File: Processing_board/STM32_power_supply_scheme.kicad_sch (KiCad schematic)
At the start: 16 parts

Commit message: added reset button
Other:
- company: (none) -> N-Pulse
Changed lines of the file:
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@@
 	(generator_version "9.0")
 	(paper "A4")
+	(title_block
+		(company "N-Pulse")
+	)
 	(text "Correct to connect VDDA to VDD ?\n\"The VDDA voltage level is independent from the VDD voltage\n and must be connected to VDD (preferably) or to VSS pin when\n these peripherals are not used.\" datasheet p29\n"
 		(exclude_from_sim no)

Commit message: 3 RF antennas
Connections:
- net 3.3V renamed +3.3V
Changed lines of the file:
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@@
-		)
-	)
-	(global_label "3.3V"
-		(shape input)
-		(at 83.82 24.13 90)
-		(fields_autoplaced yes)
-		(effects
-			(font
-				(size 1.27 1.27)
-			)
-			(justify left)
-		)
-		(property "Intersheetrefs" "${INTERSHEET_REFS}"
-			(at 83.82 17.0324 90)
-			(effects
-				(font
-					(size 1.27 1.27)
-				)
-				(justify left)
-				(hide yes)
-			)
 		)
 	)
@@
 					(unit 1)
 				)
+			)
+		)
+	)
+	(symbol
+		(lib_id "power:+3.3V")
+		(at 83.82 24.13 0)
+		(unit 1)
+		(exclude_from_sim no)
+		(in_bom yes)
+		(on_board yes)
+		(dnp no)
+		(fields_autoplaced yes)
+		(property "Reference" "#PWR046"
+			(at 83.82 27.94 0)
+			(effects
+				(font
+					(size 1.27 1.27)
+				)
+				(hide yes)
+			)
+		)
+		(property "Value" "+3.3V"
+			(at 83.82 19.05 0)
+			(effects
+				(font
+					(size 1.27 1.27)
+				)
+			)
+		)
+		(property "Footprint" ""
+			(at 83.82 24.13 0)
+			(effects
+				(font
+					(size 1.27 1.27)
+				)
+				(hide yes)
+			)
+		)
+		(property "Datasheet" ""
+			(at 83.82 24.13 0)
+			(effects
+				(font
+					(size 1.27 1.27)
+				)
+				(hide yes)
+			)
+		)
+		(property "Description" "Power symbol creates a global label with name \"+3.3V\""
+			(at 83.82 24.13 0)
+			(effects
+				(font
+					(size 1.27 1.27)
+				)
+				(hide yes)
+			)
+		)
+		(pin "1"
+		)
+		(instances
+			(project "Processing_board"
+				(path "/b48cfd4a-6c36-4270-b2b4-45cb26e35477/dd373a49-14d9-4e57-878b-300a3ee89b4f"
+					(reference "#PWR046")
+					(unit 1)
+				)

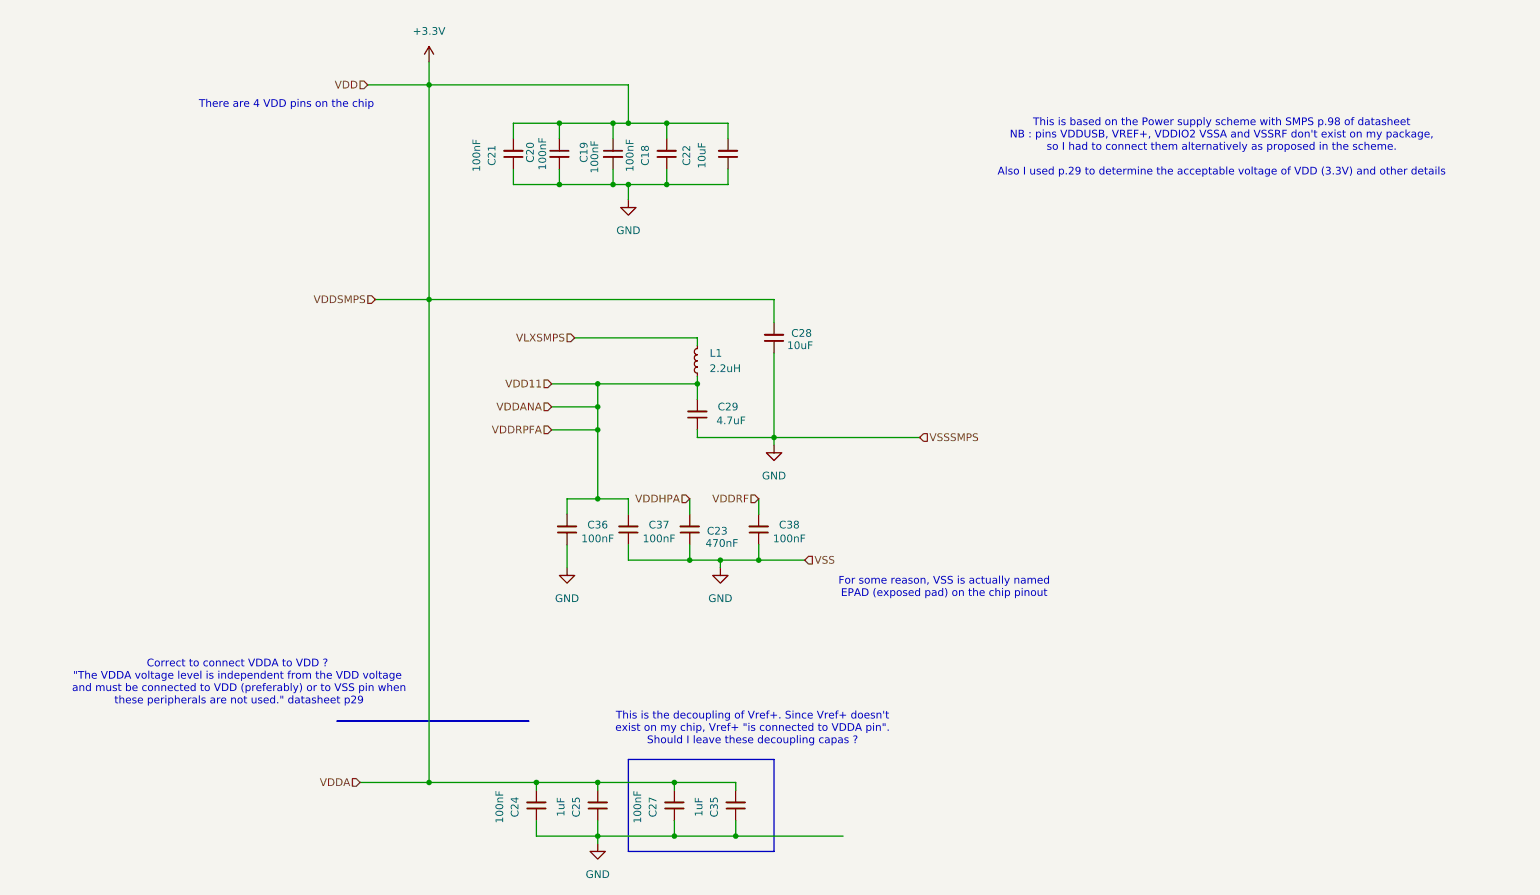
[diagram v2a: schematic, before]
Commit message: added all footprints, ready (?) to design PCB
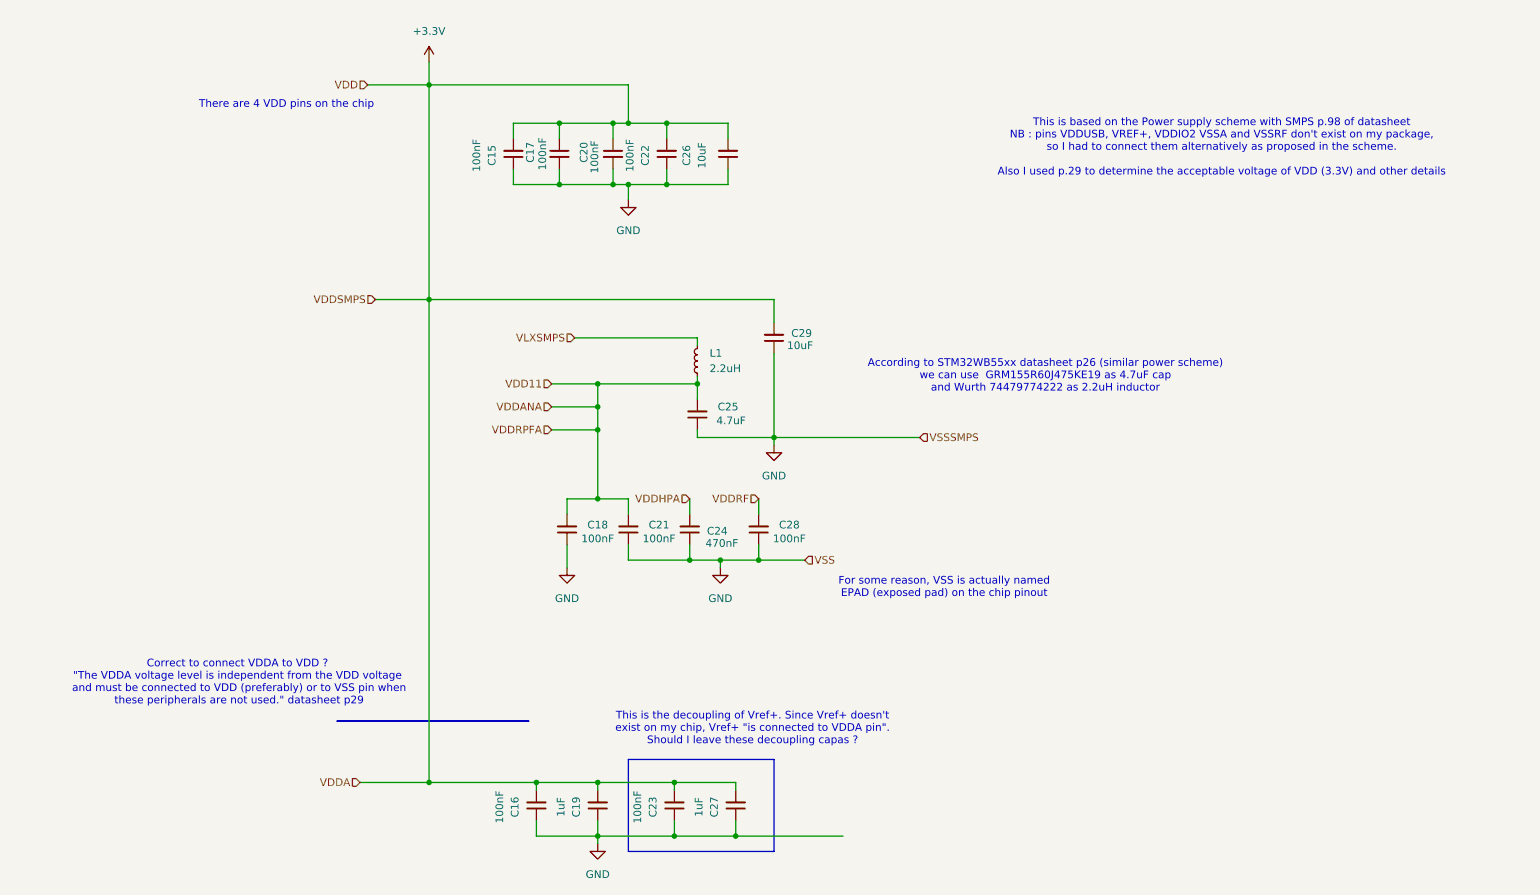
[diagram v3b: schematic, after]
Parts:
- C15: renamed from C21; footprint (none) -> Capacitor_SMD:C_0402_1005Metric
- C16: renamed from C24; footprint (none) -> Capacitor_SMD:C_0402_1005Metric
- C17: renamed from C20; footprint (none) -> Capacitor_SMD:C_0402_1005Metric
- C18: renamed from C36; footprint (none) -> Capacitor_SMD:C_0402_1005Metric
- C19: renamed from C25; footprint (none) -> Capacitor_SMD:C_0402_1005Metric
- C20: renamed from C19; footprint (none) -> Capacitor_SMD:C_0402_1005Metric
- C21: renamed from C37; footprint (none) -> Capacitor_SMD:C_0402_1005Metric
- C22: renamed from C18; footprint (none) -> Capacitor_SMD:C_0402_1005Metric
- C23: renamed from C27; footprint (none) -> Capacitor_SMD:C_0402_1005Metric
- C24: renamed from C23; footprint (none) -> Capacitor_SMD:C_0402_1005Metric
- C25: renamed from C29; footprint (none) -> Capacitor_SMD:C_0402_1005Metric
- C26: renamed from C22; footprint (none) -> Capacitor_SMD:C_0402_1005Metric
- C27: renamed from C35; footprint (none) -> Capacitor_SMD:C_0402_1005Metric
- C28: renamed from C38; footprint (none) -> Capacitor_SMD:C_0402_1005Metric
- C29: renamed from C28; footprint (none) -> Capacitor_SMD:C_0402_1005Metric
- L1: footprint (none) -> Inductor_SMD:L_0805_2012Metric
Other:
- note added: "According to STM32WB55xx datasheet p26 (similar power scheme) we can use GRM155R60J475KE19 as 4.7uF cap and Wurth 74479774222 as 2.2uH inductor"

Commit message: first draft of PCB almost done
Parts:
- removed C23: 100nF, Capacitor_SMD:C_0402_1005Metric, symbol Device:C_Small
- removed C27: 1uF, Capacitor_SMD:C_0402_1005Metric, symbol Device:C_Small
- renumbered C24 to C23, C25 to C24, C26 to C25, C28 to C26, C29 to C27
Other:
- note removed: "This is the decoupling of Vref+. Since Vref+ doesn't exist on my chip, Vref+ "is connected to VDDA pin". Should I leave these decoupling capas ?"
- moved on the sheet: C18

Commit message: more minor cleanup
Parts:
- renumbered C18 to C17, C17 to C18
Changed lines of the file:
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@@
 		(dnp no)
 		(fields_autoplaced yes)
-		(property "Reference" "#PWR066"
+		(property "Reference" "#PWR032"
 			(at 83.82 63.5 0)
 			(effects
@@
 			(project "Processing_board"
 				(path "/b48cfd4a-6c36-4270-b2b4-45cb26e35477/dd373a49-14d9-4e57-878b-300a3ee89b4f"
-					(reference "#PWR066")
+					(reference "#PWR032")
 					(unit 1)
 				)
@@
 		(dnp no)
 		(fields_autoplaced yes)
-		(property "Reference" "#PWR031"
+		(property "Reference" "#PWR034"
 			(at 104.14 114.3 0)
 			(effects
@@
 			(project "Processing_board"
 				(path "/b48cfd4a-6c36-4270-b2b4-45cb26e35477/dd373a49-14d9-4e57-878b-300a3ee89b4f"
-					(reference "#PWR031")
+					(reference "#PWR034")
 					(unit 1)
 				)
@@
 		(on_board yes)
 		(dnp no)
-		(property "Reference" "C18"
+		(property "Reference" "C17"
 			(at 109.22 100.838 0)
 			(effects
@@
 			(project "Processing_board"
 				(path "/b48cfd4a-6c36-4270-b2b4-45cb26e35477/dd373a49-14d9-4e57-878b-300a3ee89b4f"
-					(reference "C18")
+					(reference "C17")
 					(unit 1)
 				)
@@
 		(dnp no)
 		(fields_autoplaced yes)
-		(property "Reference" "#PWR035"
+		(property "Reference" "#PWR038"
 			(at 140.97 93.98 0)
 			(effects
@@
 			(project "Processing_board"
 				(path "/b48cfd4a-6c36-4270-b2b4-45cb26e35477/dd373a49-14d9-4e57-878b-300a3ee89b4f"
-					(reference "#PWR035")
+					(reference "#PWR038")
 					(unit 1)
 				)
@@
 		(dnp no)
 		(fields_autoplaced yes)
-		(property "Reference" "#PWR032"
+		(property "Reference" "#PWR035"
 			(at 106.68 160.02 0)
 			(effects
@@
 			(project "Processing_board"
 				(path "/b48cfd4a-6c36-4270-b2b4-45cb26e35477/dd373a49-14d9-4e57-878b-300a3ee89b4f"
-					(reference "#PWR032")
+					(reference "#PWR035")
 					(unit 1)
 				)
@@
 		(dnp no)
 		(fields_autoplaced yes)
-		(property "Reference" "#PWR030"
+		(property "Reference" "#PWR031"
 			(at 83.82 27.94 0)
 			(effects
@@
 			(project "Processing_board"
 				(path "/b48cfd4a-6c36-4270-b2b4-45cb26e35477/dd373a49-14d9-4e57-878b-300a3ee89b4f"
-					(reference "#PWR030")
+					(reference "#PWR031")
 					(unit 1)
 				)
@@
 		(dnp no)
 		(fields_autoplaced yes)
-		(property "Reference" "#PWR067"
+		(property "Reference" "#PWR033"
 			(at 83.82 144.78 0)
 			(effects
@@
 			(project "Processing_board"
 				(path "/b48cfd4a-6c36-4270-b2b4-45cb26e35477/dd373a49-14d9-4e57-878b-300a3ee89b4f"
-					(reference "#PWR067")
+					(reference "#PWR033")
 					(unit 1)
 				)
@@
 		(dnp no)
 		(fields_autoplaced yes)
-		(property "Reference" "#PWR033"
+		(property "Reference" "#PWR036"
 			(at 116.84 53.34 0)
 			(effects
@@
 			(project "Processing_board"
 				(path "/b48cfd4a-6c36-4270-b2b4-45cb26e35477/dd373a49-14d9-4e57-878b-300a3ee89b4f"
-					(reference "#PWR033")
+					(reference "#PWR036")
 					(unit 1)
 				)
@@
 		(on_board yes)
 		(dnp no)
-		(property "Reference" "C17"
+		(property "Reference" "C18"
 			(at 100.584 39.116 90)
 			(effects
@@
 			(project "Processing_board"
 				(path "/b48cfd4a-6c36-4270-b2b4-45cb26e35477/dd373a49-14d9-4e57-878b-300a3ee89b4f"
-					(reference "C17")
+					(reference "C18")
 					(unit 1)
 				)
@@
 		(dnp no)
 		(fields_autoplaced yes)
-		(property "Reference" "#PWR034"
+		(property "Reference" "#PWR037"
 			(at 132.08 114.3 0)
 			(effects
@@
 			(project "Processing_board"
 				(path "/b48cfd4a-6c36-4270-b2b4-45cb26e35477/dd373a49-14d9-4e57-878b-300a3ee89b4f"
-					(reference "#PWR034")
-					(unit 1)
-				)
+					(reference "#PWR037")
+					(unit 1)
+				)

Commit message: more cleanup
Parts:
- renumbered C15 to C71, C16 to C73, C17 to C74, C18 to C75, C19 to C78, C20 to C79, C21 to C80, C22 to C81, C23 to C82, C24 to C83, C25 to C84, C26 to C86, C27 to C88, L1 to L5
